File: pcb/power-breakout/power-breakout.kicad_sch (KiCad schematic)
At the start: 24 parts, among them J1 COMBO_POWER_JACK, J2 Conn_01x04_Pin, U1 FDS4435BZ, U2 FDS4435BZ

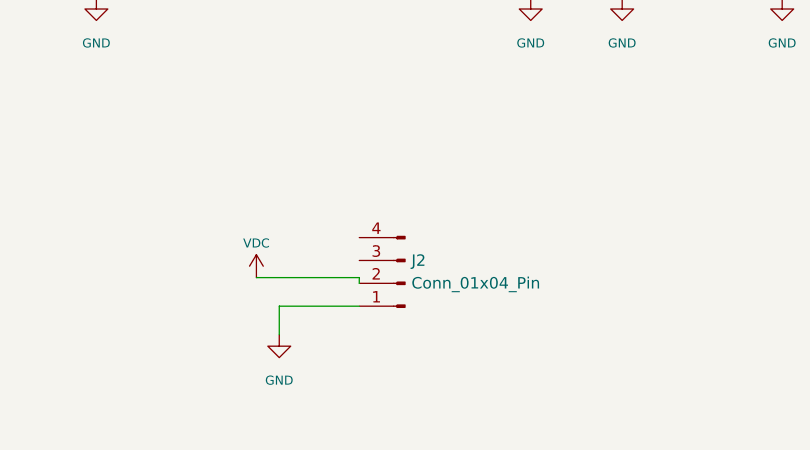
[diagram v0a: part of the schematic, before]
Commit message: updates part source for breakout, updates silkscreen
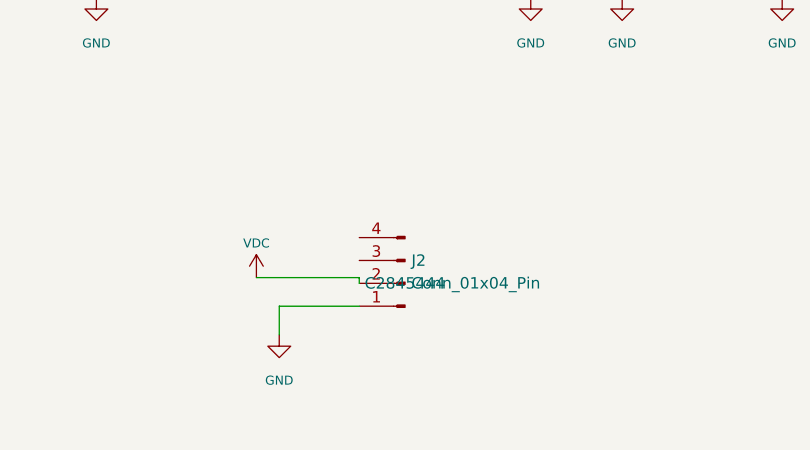
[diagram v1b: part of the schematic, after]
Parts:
- J2: LCSC (none) -> C2845444
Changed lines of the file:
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@@
+			)
+		)
+		(property "LCSC" "C2845444"
+			(at 179.07 100.965 0)
+			(effects
+				(font
+					(size 1.27 1.27)
+				)
 			)
 		)
